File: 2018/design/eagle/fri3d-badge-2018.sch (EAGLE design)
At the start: 64 parts

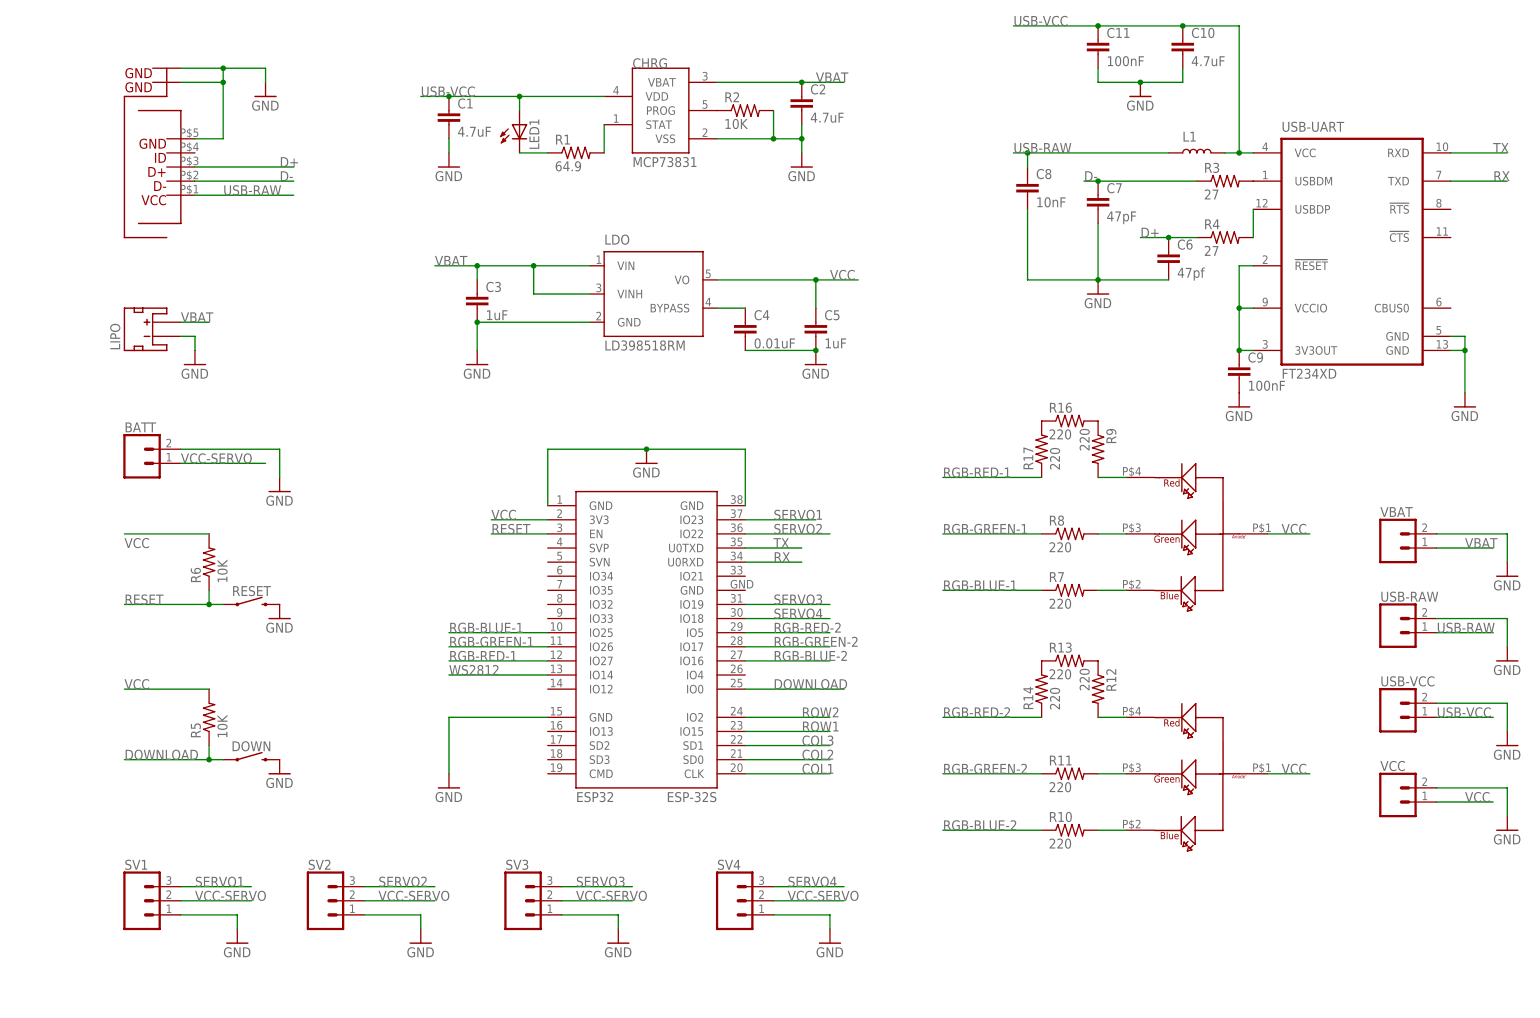
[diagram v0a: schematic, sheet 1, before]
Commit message: added functional sections to schematic
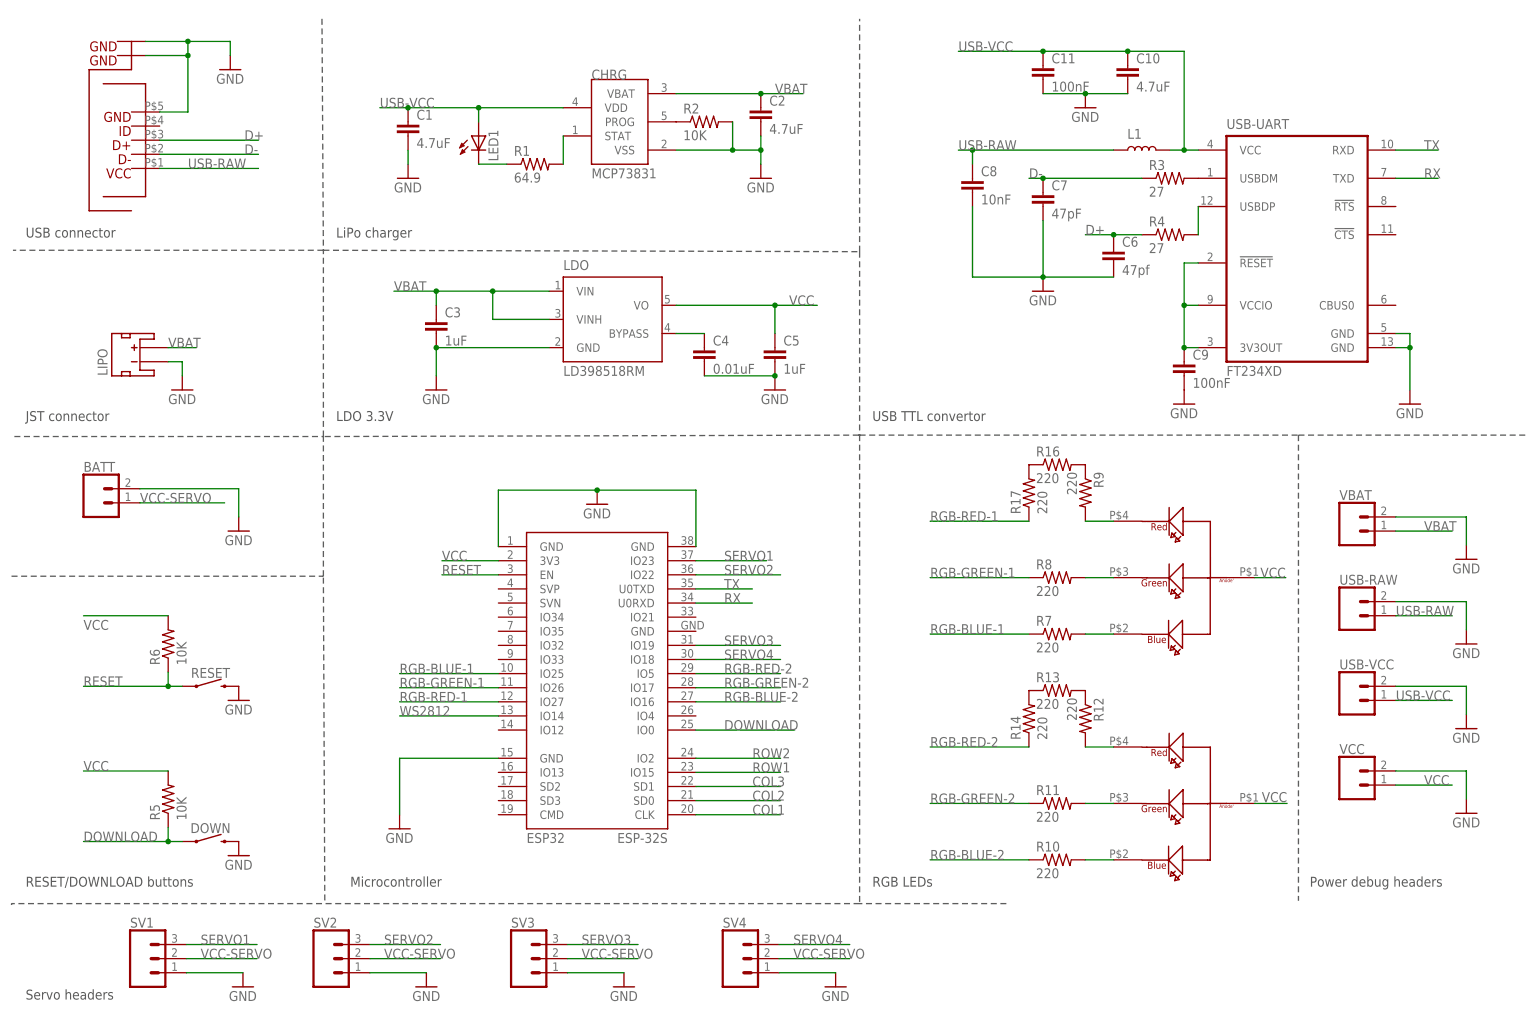
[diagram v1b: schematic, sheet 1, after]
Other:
- note added: "JST connector"
- note added: "LDO 3.3V"
- note added: "LED array"
- note added: "LiPo charger"
- note added: "Microcontroller"
- note added: "Power debug headers"
- note added: "RESET/DOWNLOAD buttons"
- note added: "RGB LEDs"
- note added: "Servo headers"
- note added: "USB TTL convertor"
- note added: "USB connector"
- note added: "WS2812 addressable LEDs"
- moved on the sheet: BATT, C1, C10, C11, C2, C3, C4, C5, C6, C7, C8, C9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

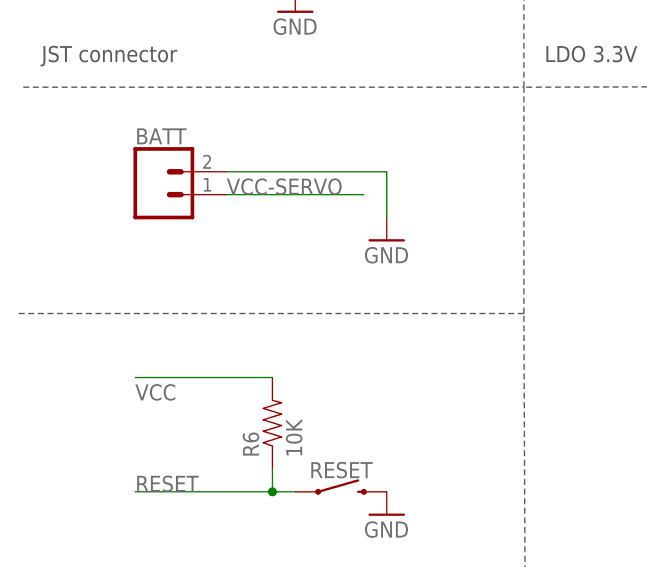
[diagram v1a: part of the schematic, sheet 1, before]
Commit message: added missing section title
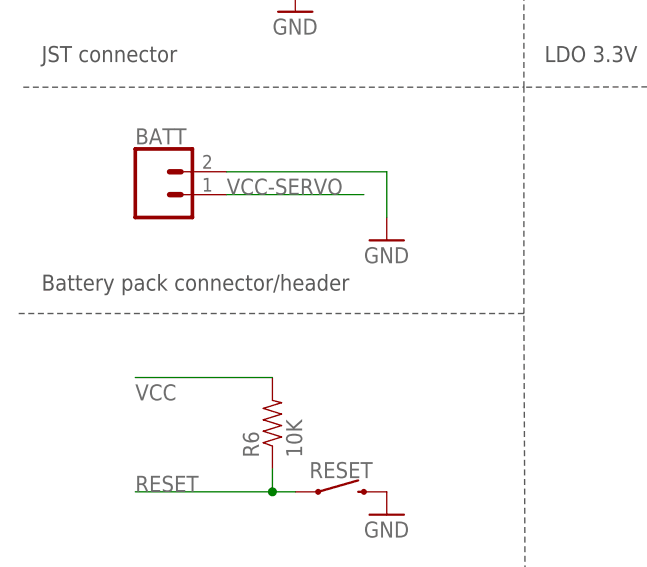
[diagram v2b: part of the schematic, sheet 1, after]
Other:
- note added: "Battery pack connector/header"
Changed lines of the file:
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@@
 <text x="2.54" y="2.54" size="1.778" layer="97">Servo headers</text>
 <text x="233.68" y="22.86" size="1.778" layer="97">Power debug headers</text>
+<text x="2.54" y="81.28" size="1.778" layer="97">Battery pack connector/header</text>
 </plain>
 <instances>
